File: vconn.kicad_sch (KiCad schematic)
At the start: 1 part, among them U7 TCPP02-M18

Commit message: WIP on vconn
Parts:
- added C31, C8: 330pF, symbol Device:C
- added C32: 100nF, symbol Device:C
- added R19: 47k, symbol Device:R
- added R20: 100k, symbol Device:R
- added R21: 7m, Resistor_SMD:R_0815_2038Metric_Pad1.20x4.05mm_HandSolder, symbol Device:R
- added U8: STL40DN3LLH5, symbol usb_zekers:STL40DN3LLH5
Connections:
- net TCPP_EN: now reaches U7.1 (EN)
- net TCPP_EN: now also R20.1
- net GND: now reaches U7.10 (GND)
- net GND: now also U7.14 (GND), U7.15 (I2C_ADD), U7.19 (GND), C31.2, C32.2, C8.2, R20.2
- net TCPP_CC_PORT.CC2c: now reaches U7.11 (CC2c)
- net TCPP_CC_PORT.CC2c: now also C31.1
- net at U7.12 (CBIAS): now also C32.1
- net TCPP_CC_PORT.CC1c: now reaches U7.13 (CC1c)
- net TCPP_CC_PORT.CC1c: now also C8.1
- net I2C.SDA: now reaches U7.16 (SDA)
- net I2C.SCL: now reaches U7.17 (SCL)
- net at U7.18 (FGLn): now also R19.1
- net TCPP_CC_MCU.CC1: now reaches U7.2 (CC1)
- net +3V3: now reaches U7.3 (VCC_VCONN)
- net +3V3: now also R19.2
- net TCPP_CC_MCU.CC2: now reaches U7.4 (CC2)
- net TCPP_IANA: now reaches U7.5 (IANA)
- net GATE: now reaches U7.6 (GATE)
- net GATE: now also U8.2 (G2), U8.4 (G1)
- net SRC: now reaches U7.7 (SRC)
- net SRC: now also U8.1 (S2), U8.3 (S1)
- net VBUS: now reaches U7.8 (VBUSc)
- net VBUS: now also R21.2
- net Isense: now reaches U7.9 (Isense)
- net Isense: now also R21.1, U8.5,6 (D1)
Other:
- note added: "TODO find 7mOhm, 1W shunt equivalent to ERJMP2MF7M0U, and use it for R21, R9 and R10"
- moved on the sheet: U7

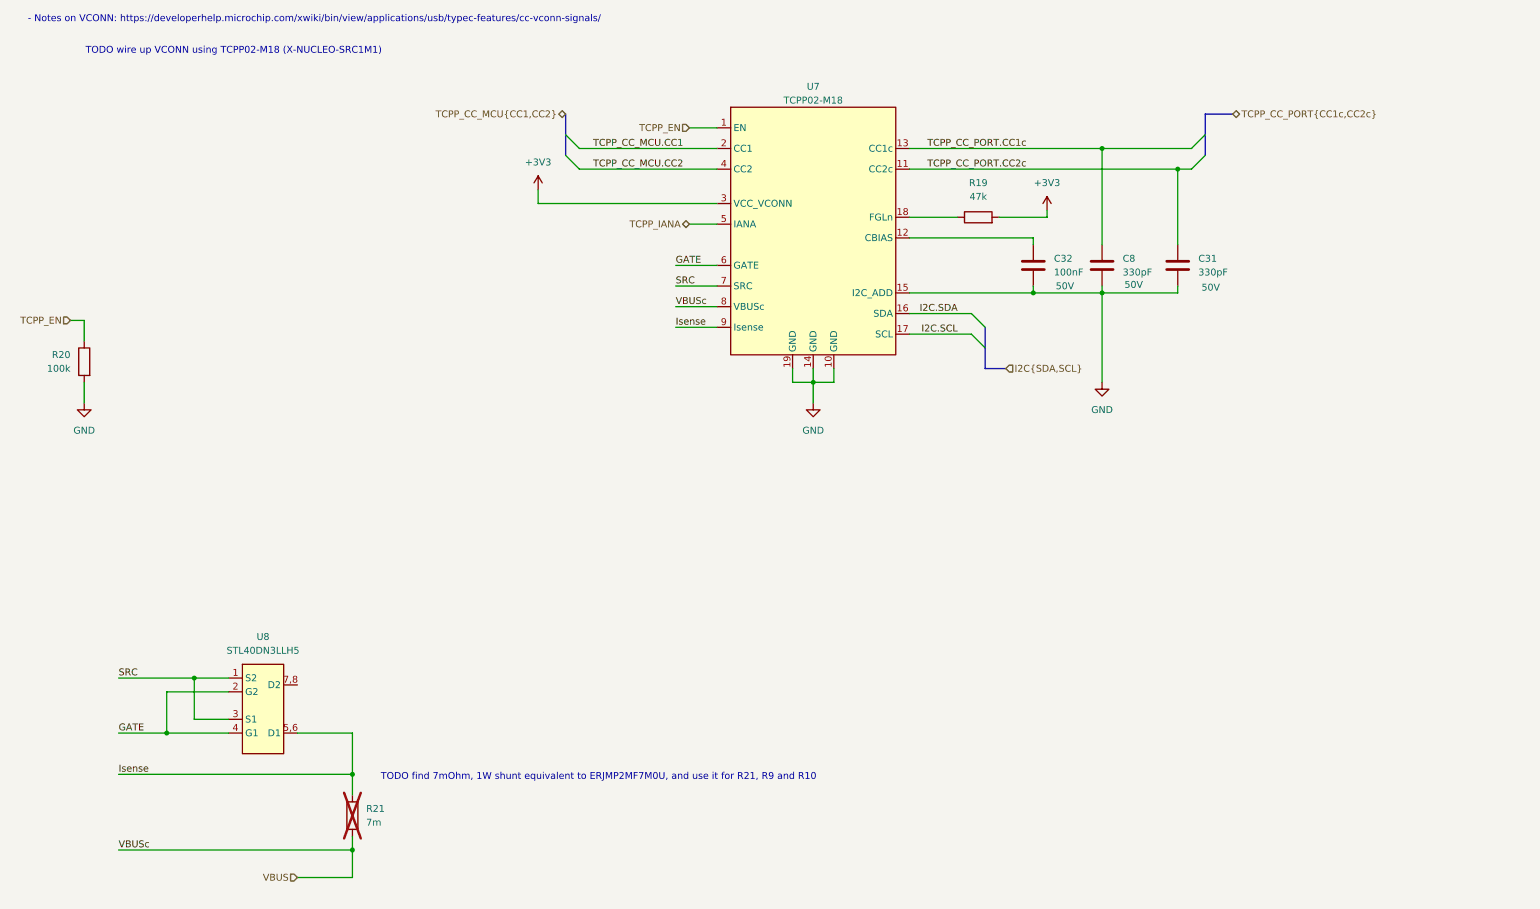
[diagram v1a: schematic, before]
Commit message: wire up vconn stuff
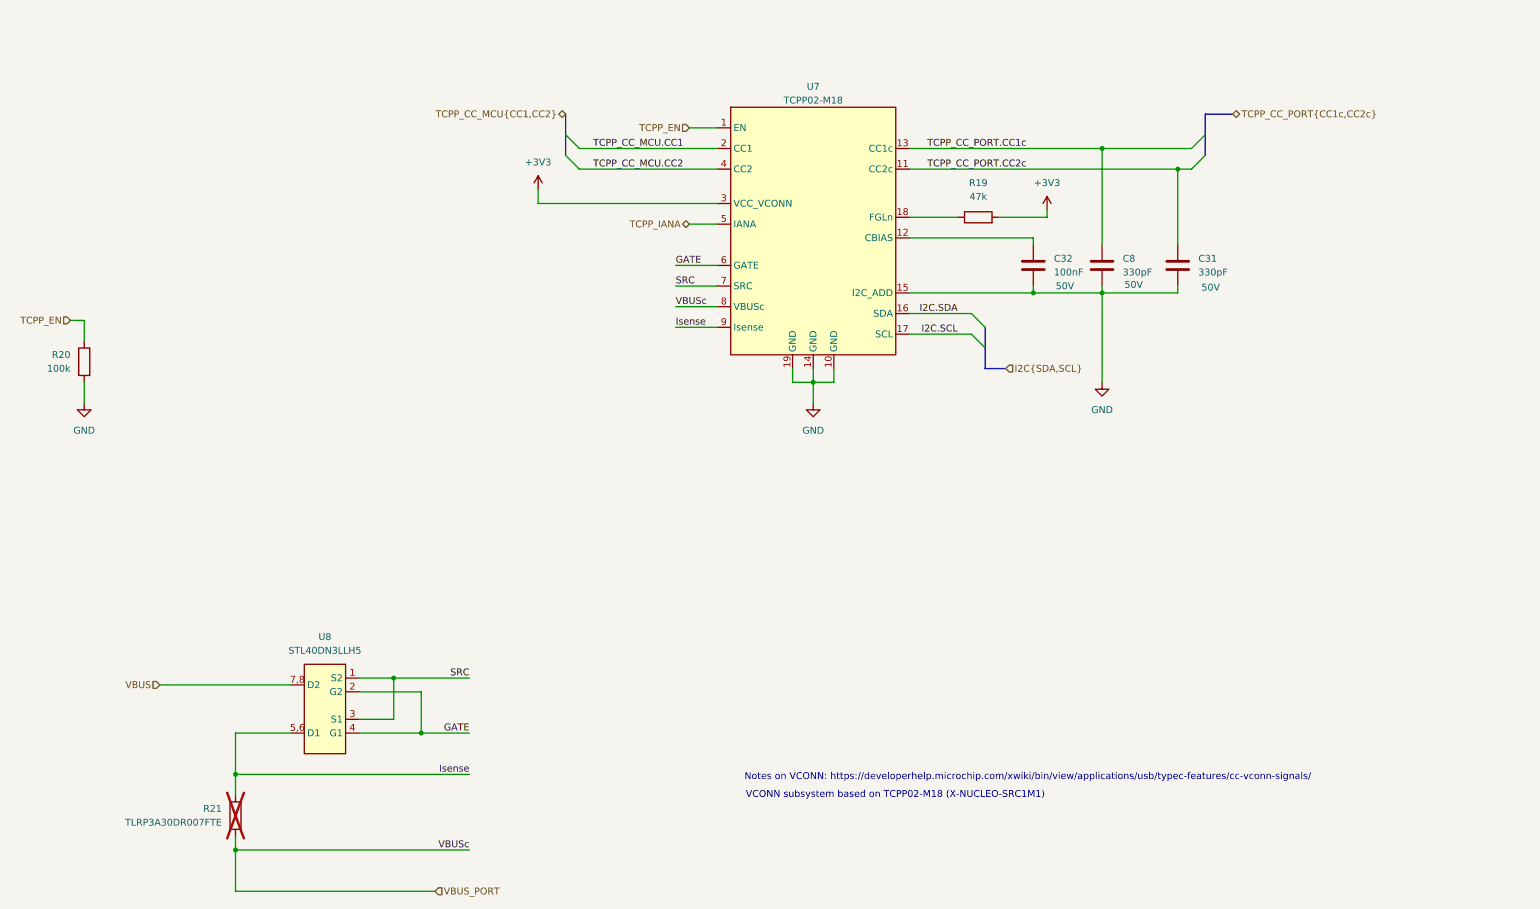
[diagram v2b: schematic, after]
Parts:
- R21: value 7m -> TLRP3A30DR007FTE; footprint Resistor_SMD:R_0815_2038Metric_Pad1.20x4.05mm_HandSolder -> Resistor_SMD:R_2512_6332Metric_Pad1.40x3.35mm_HandSolder
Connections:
- net VBUS: now also U8.7,8 (D2); no longer R21.2, U7.8 (VBUSc)
- new net VBUS_PORT: R21.2, U7.8 (VBUSc)
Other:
- note added: "Notes on VCONN: https://developerhelp.microchip.com/xwiki/bin/view/applications/usb/typec-features/cc-vconn-signals/"
- note added: "VCONN subsystem based on TCPP02-M18 (X-NUCLEO-SRC1M1)"
- note removed: "- Notes on VCONN: https://developerhelp.microchip.com/xwiki/bin/view/applications/usb/typec-features/cc-vconn-signals/"
- note removed: "TODO find 7mOhm, 1W shunt equivalent to ERJMP2MF7M0U, and use it for R21, R9 and R10"
- note removed: "TODO wire up VCONN using TCPP02-M18 (X-NUCLEO-SRC1M1)"
- moved on the sheet: R21, U8

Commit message: Wire up VCONN_FLGn
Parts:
- added TP10, TP13, TP7, TP8, TP9: TestPoint, symbol Connector:TestPoint
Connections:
- net +3V3: now also TP13.1; no longer U7.3 (VCC_VCONN)
- net TCPP_EN: now also TP8.1, TP9.1
- net TCPP_IANA: now also TP10.1
- net VBUS: now also TP7.1
- new net +5V: U7.3 (VCC_VCONN)
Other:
- moved on the sheet: R19

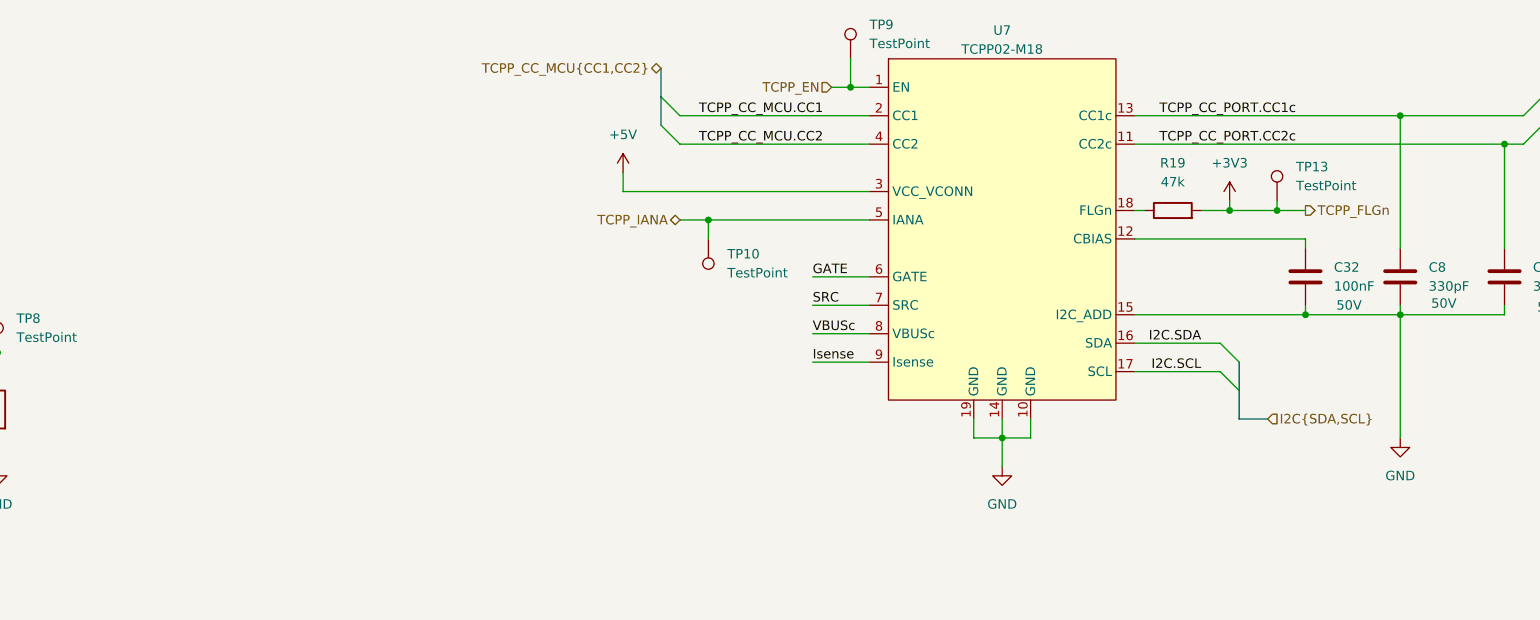
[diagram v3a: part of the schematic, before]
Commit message: Fix ERC errors, swap out mosfets for NVC chip
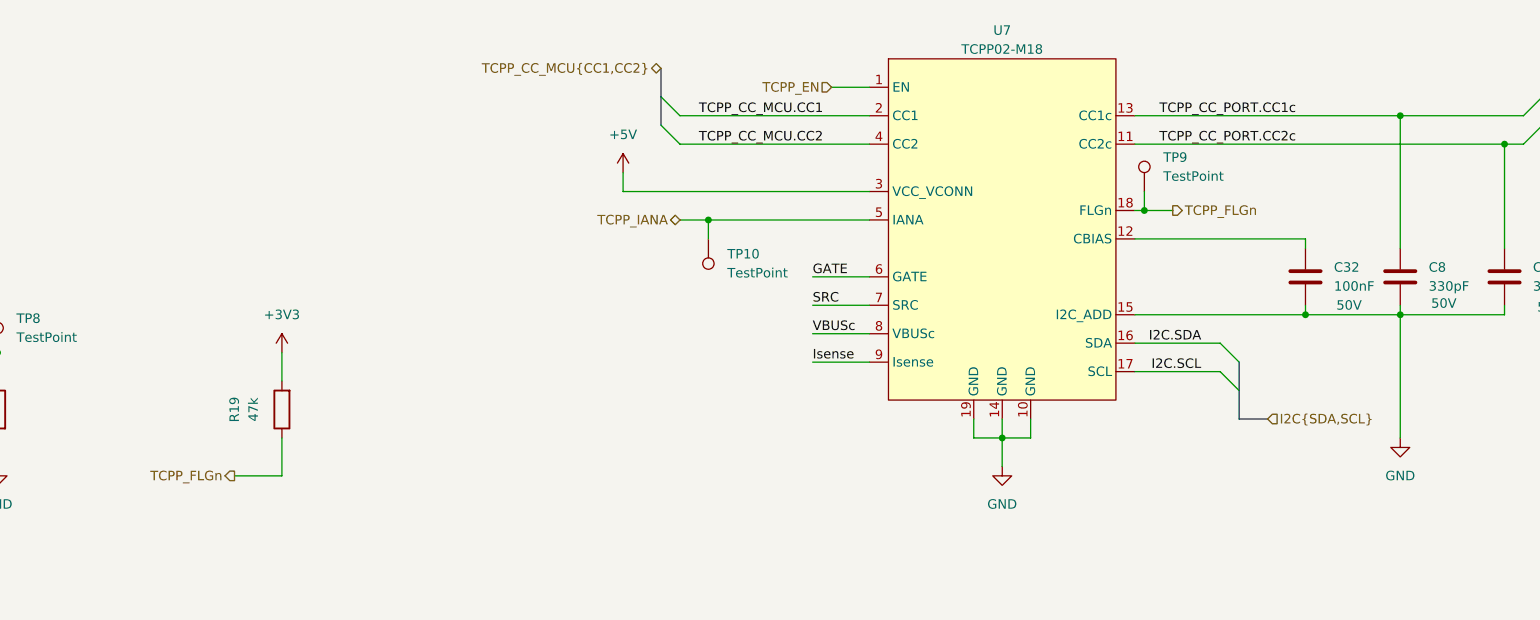
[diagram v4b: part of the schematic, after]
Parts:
- removed TP13: TestPoint, symbol Connector:TestPoint
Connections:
- net TCPP_EN: no longer TP9.1
- net TCPP_FLGn: now reaches R19.1, U7.18 (FLGn)
- net TCPP_FLGn: now also TP9.1
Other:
- moved on the sheet: R19

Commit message: more footprints
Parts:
- C31, C8: footprint (none) -> Capacitor_SMD:C_0603_1608Metric; JLCPCB Part No (none) -> C1664
- C32: footprint (none) -> Capacitor_SMD:C_1206_3216Metric; JLCPCB Part No (none) -> C24497
- TP10, TP7, TP8, TP9: footprint (none) -> TestPoint:TestPoint_Pad_D1.0mm
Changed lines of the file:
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@@
 			)
 		)
-		(property "Footprint" ""
+		(property "Footprint" "Capacitor_SMD:C_0603_1608Metric"
 			(at 240.9952 68.58 0)
 			(effects
@@
 			)
 		)
-		(property "JLCPCB Part No" ""
+		(property "JLCPCB Part No" "C1664"
 			(at 240.03 64.77 0)
 			(effects
@@
 			)
 		)
-		(property "Footprint" ""
+		(property "Footprint" "Capacitor_SMD:C_0603_1608Metric"
 			(at 227.0252 68.58 0)
 			(effects
@@
 			)
 		)
-		(property "JLCPCB Part No" ""
+		(property "JLCPCB Part No" "C1664"
 			(at 226.06 64.77 0)
 			(effects
@@
 			)
 		)
-		(property "Footprint" ""
+		(property "Footprint" "TestPoint:TestPoint_Pad_D1.0mm"
 			(at 196.85 53.34 0)
 			(effects
@@
 			)
 		)
-		(property "Footprint" ""
+		(property "Footprint" "TestPoint:TestPoint_Pad_D1.0mm"
 			(at 128.27 59.69 0)
 			(effects
@@
 			)
 		)
-		(property "Footprint" ""
+		(property "Footprint" "Capacitor_SMD:C_1206_3216Metric"
 			(at 214.3252 68.58 0)
 			(effects
@@
 			)
 		)
-		(property "JLCPCB Part No" ""
+		(property "JLCPCB Part No" "C24497"
 			(at 213.36 64.77 0)
 			(effects
@@
 			)
 		)
-		(property "Footprint" ""
+		(property "Footprint" "TestPoint:TestPoint_Pad_D1.0mm"
 			(at 66.04 142.24 0)
 			(effects
@@
 			)
 		)
-		(property "Footprint" ""
+		(property "Footprint" "TestPoint:TestPoint_Pad_D1.0mm"
 			(at 43.18 74.93 0)
 			(effects
